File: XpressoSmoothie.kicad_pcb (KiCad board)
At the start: 2 copper layers, 99.7 x 99.7 mm, 130 parts, among them J1 HEADER_4, J10 HEADER_3X2, J11 Pwr_in, J12 HEADER_4, J13 HEADER_4X2, J14 HEADER_3X2, J15 HEADER_4, J16 HEADER_4, J17 HEADER_4, J172 HEADER_2, J18 HEADER_4, J19 HEADER_2, J2 HEADER_4, J20 HEADER_2, J21 HEADER_2, J22 HEADER_2, J23 HEADER_4, J232 HEADER_2, J24 HEADER_4, J25 HEADER_4, J252 HEADER_2, J26 USB, J27 HEADER_4, J28 MICROSD-MOLEX, J3 HEADER_3, J4 HEADER_3X2, J5 HEADER_3X2, J6 LPCXPRESSO_GENERIC_HEADER, J7 HEADER_4, J8 HEADER_4, J9 HEADER_3X2, M1 LOGO_OSHW, M2 LOGO_OSHW, Q1 IRLB 8743, Q2 IRLB 8743, Q3 IRLB 8743, Q4 IRLB 8743, SW1 SW_PUSH, SW2 SW_PUSH, U1 POLOLU_A4988, U10 TC4422A, U11 TC4422A, U12 LM1117-3.3, U2 POLOLU_A4988, U3 POLOLU_A4988, U4 POLOLU_A4988, U5 POLOLU_A4988, U7 LM7809CT, U8 TC4422A, U9 TC4422A

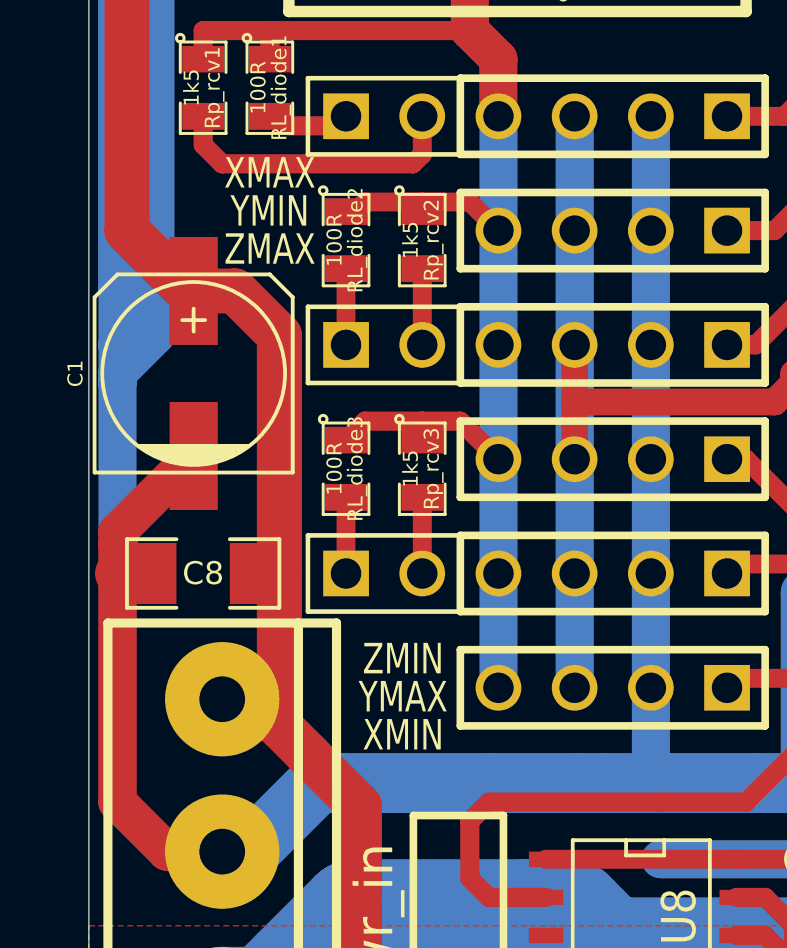
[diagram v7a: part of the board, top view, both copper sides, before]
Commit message: Switched around endstop names so they're in order going top to bottom.
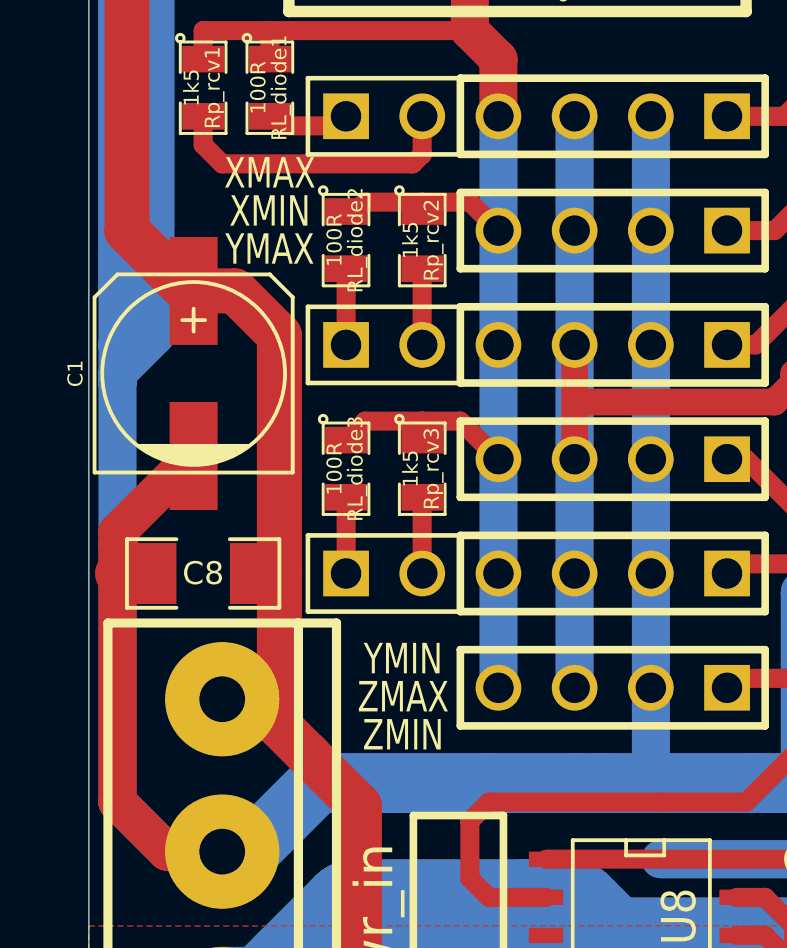
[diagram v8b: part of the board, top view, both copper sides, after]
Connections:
- J16 pad 1: XMIN -> ZMIN
- J18 pad 1: YMIN -> XMIN
- J23 pad 1: YMAX -> ZMAX
- J24 pad 1: ZMIN -> YMIN
- J25 pad 1: ZMAX -> YMAX
- J6 pad 22: ZMAX -> YMAX
- J6 pad 23: YMIN -> XMIN
- J6 pad 50: XMIN -> ZMIN
- J6 pad 51: YMAX -> ZMAX
- J6 pad 52: ZMIN -> YMIN
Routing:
- net ZMAX: track 27.2 -> 14.3 mm
- net YMAX: track 14.3 -> 27.2 mm
- net YMIN: track 22.7 -> 12.2 mm
- net ZMIN: track 12.2 -> 18.3 mm
- net XMIN: track 18.3 -> 22.7 mm
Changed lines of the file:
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@@
     (links 344)
     (no_connects 11)
-    (area 56.388 52.51262 179.864657 163.2712)
+    (area 71.742299 53.962299 171.462701 153.682701)
     (thickness 1.6)
     (drawings 36)
@@
   (layers
     (15 F.Cu signal)
-    (0 B.Cu signal hide)
+    (0 B.Cu signal)
     (16 B.Adhes user)
     (17 F.Adhes user)
@@
     (pad 52 thru_hole oval (at 64.77 -29.21 270) (size 2.54 1.524) (drill 1.016)
       (layers *.Cu *.Mask F.SilkS)
-      (net 138 ZMIN)
+      (net 133 YMIN)
     )
     (pad 51 thru_hole oval (at 62.23 -29.21 270) (size 2.54 1.524) (drill 1.016)
       (layers *.Cu *.Mask F.SilkS)
-      (net 132 YMAX)
+      (net 137 ZMAX)
     )
     (pad 50 thru_hole oval (at 59.69 -29.21 270) (size 2.54 1.524) (drill 1.016)
       (layers *.Cu *.Mask F.SilkS)
-      (net 129 XMIN)
+      (net 138 ZMIN)
     )
     (pad 23 thru_hole oval (at 59.69 -6.35 270) (size 2.54 1.524) (drill 1.016)
       (layers *.Cu *.Mask F.SilkS)
-      (net 133 YMIN)
+      (net 129 XMIN)
     )
     (pad 24 thru_hole oval (at 62.23 -6.35 270) (size 2.54 1.524) (drill 1.016)
@@
     (pad 22 thru_hole oval (at 57.15 -6.35 270) (size 2.54 1.524) (drill 1.016)
       (layers *.Cu *.Mask F.SilkS)
-      (net 137 ZMAX)
+      (net 132 YMAX)
     )
     (pad 21 thru_hole oval (at 54.61 -6.35 270) (size 2.54 1.524) (drill 1.016)
@@
     (pad 1 thru_hole rect (at -3.81 0 180) (size 1.524 1.524) (drill 1.016)
       (layers *.Cu *.Mask F.SilkS)
-      (net 129 XMIN)
+      (net 138 ZMIN)
     )
     (pad 2 thru_hole circle (at -1.27 0 180) (size 1.524 1.524) (drill 1.016)
@@
     (pad 1 thru_hole rect (at -3.81 0 180) (size 1.524 1.524) (drill 1.016)
       (layers *.Cu *.Mask F.SilkS)
-      (net 133 YMIN)
+      (net 129 XMIN)
     )
     (pad 2 thru_hole circle (at -1.27 0 180) (size 1.524 1.524) (drill 1.016)
@@
     (pad 1 thru_hole rect (at -3.81 0 180) (size 1.524 1.524) (drill 1.016)
       (layers *.Cu *.Mask F.SilkS)
-      (net 138 ZMIN)
+      (net 133 YMIN)
     )
     (pad 2 thru_hole circle (at -1.27 0 180) (size 1.524 1.524) (drill 1.016)
@@
     (pad 1 thru_hole rect (at -3.81 0 180) (size 1.524 1.524) (drill 1.016)
       (layers *.Cu *.Mask F.SilkS)
-      (net 132 YMAX)
+      (net 137 ZMAX)
     )
     (pad 2 thru_hole circle (at -1.27 0 180) (size 1.524 1.524) (drill 1.016)
@@
     (pad 1 thru_hole rect (at -3.81 0 180) (size 1.524 1.524) (drill 1.016)
       (layers *.Cu *.Mask F.SilkS)
-      (net 137 ZMAX)
+      (net 132 YMAX)
     )
     (pad 2 thru_hole circle (at -1.27 0 180) (size 1.524 1.524) (drill 1.016)
@@
     (effects (font (size 1.016 0.762) (thickness 0.1524)))
   )
-  (gr_text ZMIN (at 82.2325 124.1425) (layer F.SilkS)
+  (gr_text YMIN (at 82.2325 124.1425) (layer F.SilkS)
     (effects (font (size 1.016 0.762) (thickness 0.1524)))
   )
-  (gr_text YMIN (at 77.7875 109.22) (layer F.SilkS)
+  (gr_text XMIN (at 77.7875 109.22) (layer F.SilkS)
     (effects (font (size 1.016 0.762) (thickness 0.1524)))
   )
-  (gr_text XMIN (at 82.2325 126.6825) (layer F.SilkS)
+  (gr_text ZMIN (at 82.2325 126.6825) (layer F.SilkS)
     (effects (font (size 1.016 0.762) (thickness 0.1524)))
   )
-  (gr_text ZMAX (at 77.7875 110.49) (layer F.SilkS)
+  (gr_text YMAX (at 77.7875 110.49) (layer F.SilkS)
     (effects (font (size 1.016 0.762) (thickness 0.1524)))
   )
-  (gr_text YMAX (at 82.2325 125.4125) (layer F.SilkS)
+  (gr_text ZMAX (at 82.2325 125.4125) (layer F.SilkS)
     (effects (font (size 1.016 0.762) (thickness 0.1524)))
   )
@@
     (arrow2b (pts (xy 64.770001 53.975) (xy 65.356421 55.101503)))
   )
-  (segment (start 164.475 102.955) (end 170.688 102.955) (width 0.635) (layer F.Cu) (net 1) (status 400000))
+  (segment (start 164.475 102.955) (end 170.688 102.955) (width 0.635) (layer F.Cu) (net 1))
   (segment (start 170.688 102.955) (end 170.688 102.912) (width 0.635) (layer F.Cu) (net 1))
   (segment (start 170.688 109.982) (end 170.688 111.125) (width 0.889) (layer F.Cu) (net 1))
@@
   (segment (start 94.9325 106.045) (end 93.0275 106.045) (width 0.635) (layer F.Cu) (net 128))
   (segment (start 104.775 96.2025) (end 94.9325 106.045) (width 0.635) (layer F.Cu) (net 128))
-  (segment (start 95.5675 124.7775) (end 93.345 124.7775) (width 0.635) (layer F.Cu) (net 129))
-  (segment (start 107.315 116.84) (end 107.315 117.7925) (width 0.635) (layer F.Cu) (net 129))
-  (segment (start 100.33 124.7775) (end 107.315 117.7925) (width 0.635) (layer F.Cu) (net 129))
-  (segment (start 95.5675 124.7775) (end 100.33 124.7775) (width 0.635) (layer F.Cu) (net 129))
-  (segment (start 93.345 124.7775) (end 93.0275 125.095) (width 0.635) (layer F.Cu) (net 129))
+  (segment (start 93.0275 109.855) (end 94.615 109.855) (width 0.635) (layer F.Cu) (net 129))
+  (segment (start 107.315 97.155) (end 94.615 109.855) (width 0.635) (layer F.Cu) (net 129))
+  (segment (start 107.315 97.155) (end 107.315 93.98) (width 0.635) (layer F.Cu) (net 129))
   (segment (start 120.65 76.5175) (end 120.65 80.01) (width 0.635) (layer B.Cu) (net 130))
   (segment (start 117.475 83.185) (end 117.475 93.98) (width 0.635) (layer B.Cu) (net 130))
@@
   (segment (start 118.11 78.74) (end 118.11 76.5175) (width 0.635) (layer B.Cu) (net 131))
   (segment (start 114.935 81.915) (end 118.11 78.74) (width 0.635) (layer B.Cu) (net 131))
-  (segment (start 95.5675 120.9675) (end 93.345 120.9675) (width 0.635) (layer F.Cu) (net 132))
-  (segment (start 95.5675 120.9675) (end 101.9175 120.9675) (width 0.635) (layer F.Cu) (net 132))
-  (segment (start 101.9175 120.9675) (end 104.775 118.11) (width 0.635) (layer F.Cu) (net 132))
-  (segment (start 104.775 116.84) (end 104.775 118.11) (width 0.635) (layer F.Cu) (net 132))
-  (segment (start 93.345 120.9675) (end 93.0275 121.285) (width 0.635) (layer F.Cu) (net 132))
-  (segment (start 93.0275 109.855) (end 94.615 109.855) (width 0.635) (layer F.Cu) (net 133))
-  (segment (start 107.315 97.155) (end 94.615 109.855) (width 0.635) (layer F.Cu) (net 133))
-  (segment (start 107.315 97.155) (end 107.315 93.98) (width 0.635) (layer F.Cu) (net 133))
+  (segment (start 109.855 93.98) (end 109.855 97.79) (width 0.635) (layer F.Cu) (net 132))
+  (segment (start 93.98 113.665) (end 93.0275 113.665) (width 0.635) (layer F.Cu) (net 132))
+  (segment (start 109.855 97.79) (end 93.98 113.665) (width 0.635) (layer F.Cu) (net 132))
+  (segment (start 93.0275 117.475) (end 93.6625 117.475) (width 0.635) (layer F.Cu) (net 133))
+  (segment (start 102.235 118.745) (end 102.235 116.84) (width 0.635) (layer F.Cu) (net 133))
+  (segment (start 101.6 119.38) (end 102.235 118.745) (width 0.635) (layer F.Cu) (net 133))
+  (segment (start 95.5675 119.38) (end 101.6 119.38) (width 0.635) (layer F.Cu) (net 133))
+  (segment (start 93.6625 117.475) (end 95.5675 119.38) (width 0.635) (layer F.Cu) (net 133))
   (segment (start 135.255 93.98) (end 135.255 92.075) (width 0.635) (layer B.Cu) (net 134))
   (segment (start 143.51 85.4075) (end 143.51 76.5175) (width 0.635) (layer B.Cu) (net 134))
@@
   (segment (start 137.16 87.9475) (end 138.7475 87.9475) (width 0.635) (layer B.Cu) (net 136))
   (segment (start 132.715 92.3925) (end 137.16 87.9475) (width 0.635) (layer B.Cu) (net 136))
-  (segment (start 109.855 93.98) (end 109.855 97.79) (width 0.635) (layer F.Cu) (net 137))
-  (segment (start 93.98 113.665) (end 93.0275 113.665) (width 0.635) (layer F.Cu) (net 137))
-  (segment (start 109.855 97.79) (end 93.98 113.665) (width 0.635) (layer F.Cu) (net 137))
-  (segment (start 93.0275 117.475) (end 93.6625 117.475) (width 0.635) (layer F.Cu) (net 138))
-  (segment (start 102.235 118.745) (end 102.235 116.84) (width 0.635) (layer F.Cu) (net 138))
-  (segment (start 101.6 119.38) (end 102.235 118.745) (width 0.635) (layer F.Cu) (net 138))
-  (segment (start 95.5675 119.38) (end 101.6 119.38) (width 0.635) (layer F.Cu) (net 138))
-  (segment (start 93.6625 117.475) (end 95.5675 119.38) (width 0.635) (layer F.Cu) (net 138))
+  (segment (start 95.5675 120.9675) (end 93.345 120.9675) (width 0.635) (layer F.Cu) (net 137))
+  (segment (start 95.5675 120.9675) (end 101.9175 120.9675) (width 0.635) (layer F.Cu) (net 137))
+  (segment (start 101.9175 120.9675) (end 104.775 118.11) (width 0.635) (layer F.Cu) (net 137))
+  (segment (start 104.775 116.84) (end 104.775 118.11) (width 0.635) (layer F.Cu) (net 137))
+  (segment (start 93.345 120.9675) (end 93.0275 121.285) (width 0.635) (layer F.Cu) (net 137))
+  (segment (start 95.5675 124.7775) (end 93.345 124.7775) (width 0.635) (layer F.Cu) (net 138))
+  (segment (start 107.315 116.84) (end 107.315 117.7925) (width 0.635) (layer F.Cu) (net 138))
+  (segment (start 100.33 124.7775) (end 107.315 117.7925) (width 0.635) (layer F.Cu) (net 138))
+  (segment (start 95.5675 124.7775) (end 100.33 124.7775) (width 0.635) (layer F.Cu) (net 138))
+  (segment (start 93.345 124.7775) (end 93.0275 125.095) (width 0.635) (layer F.Cu) (net 138))
   (zone (net 20) (net_name GNDPWR) (layer F.Cu) (hatch edge 0.508)
     (connect_pads yes (clearance 0.635))
